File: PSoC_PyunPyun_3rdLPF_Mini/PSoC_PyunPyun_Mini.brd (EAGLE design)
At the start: 57.1 x 52.1 mm, 28 parts, among them IC1 LM358N

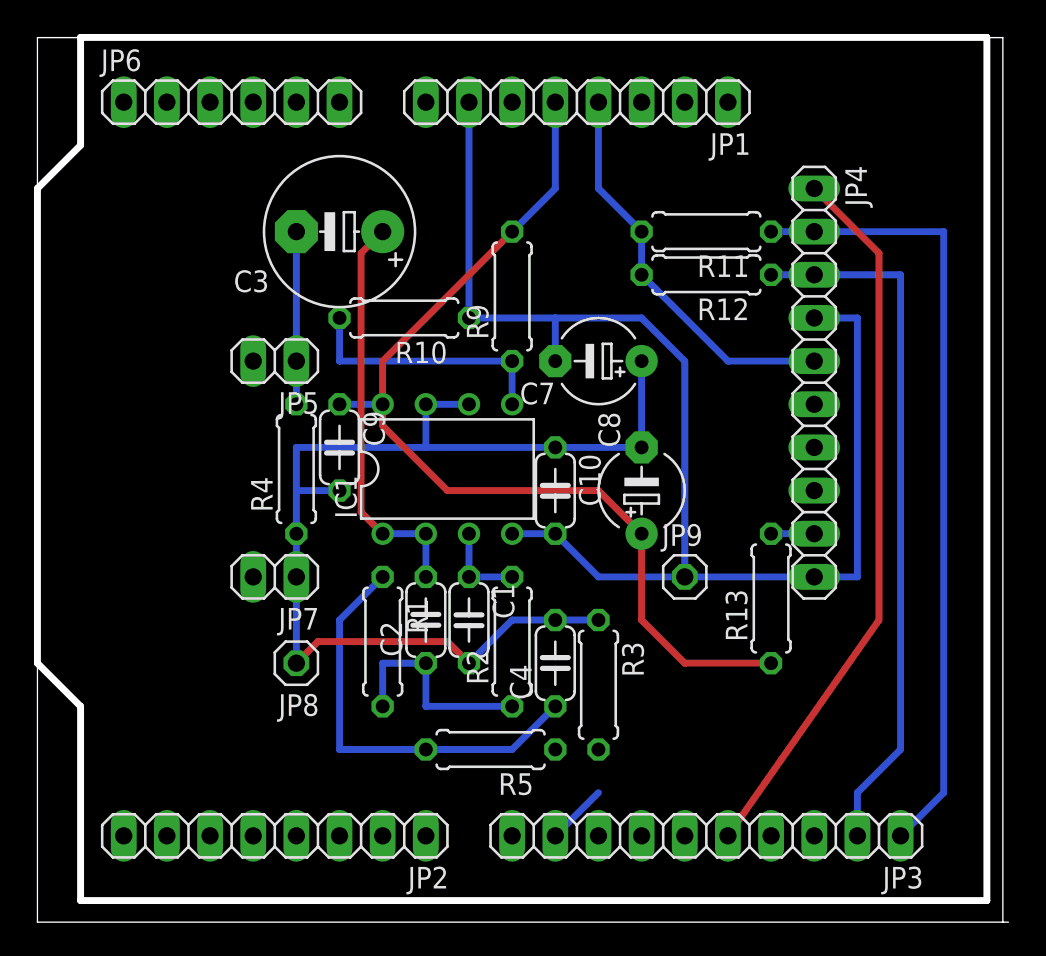
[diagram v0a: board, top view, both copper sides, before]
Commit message: PSoC_Pyun_Pyun_Mini 回路図、基板図修正
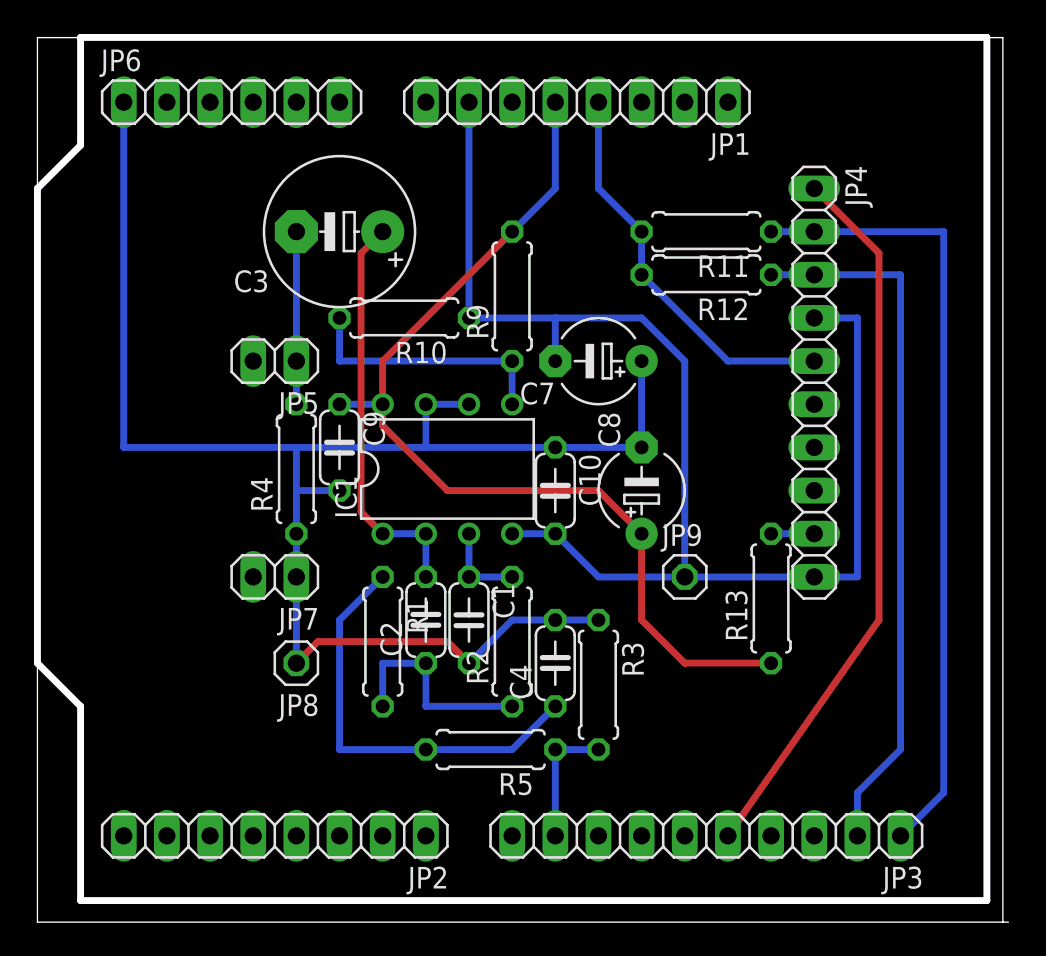
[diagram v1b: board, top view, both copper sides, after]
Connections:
- net AGND: now also JP6.1
- net IDAC7: now also JP3.8; no longer JP3.10
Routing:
- net AGND: track 65.6 -> 96.1 mm
- net IDAC8: track 3.59 -> 7.62 mm
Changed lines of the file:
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@@
 <layer number="97" name="Info" color="7" fill="1" visible="no" active="no"/>
 <layer number="98" name="Guide" color="6" fill="1" visible="no" active="no"/>
-<layer number="100" name="Grid" color="7" fill="1" visible="yes" active="yes"/>
+<layer number="100" name="Grid" color="7" fill="1" visible="no" active="yes"/>
 </layers>
 <board>
@@
 <signal name="IDAC8">
 <contactref element="JP3" pad="9"/>
-<wire x1="30.48" y1="5.08" x2="33.02" y2="7.62" width="0.4064" layer="16"/>
 <contactref element="R5" pad="1"/>
 <contactref element="R3" pad="2"/>
-<wire x1="30.48" y1="10.16" x2="33.02" y2="10.16" width="0" layer="19" extent="1-1"/>
-<wire x1="33.02" y1="7.62" x2="33.02" y2="10.16" width="0" layer="19" extent="16-16"/>
+<wire x1="33.02" y1="10.16" x2="30.48" y2="10.16" width="0.4064" layer="16"/>
+<wire x1="30.48" y1="10.16" x2="30.48" y2="5.08" width="0.4064" layer="16"/>
 </signal>
 <signal name="N$3">
@@
 <wire x1="25.4" y1="15.24" x2="27.94" y2="17.78" width="0.4064" layer="16"/>
 <wire x1="27.94" y1="17.78" x2="30.48" y2="17.78" width="0.4064" layer="16"/>
+<contactref element="JP6" pad="1"/>
+<wire x1="15.24" y1="27.94" x2="5.08" y2="27.94" width="0.4064" layer="16"/>
+<wire x1="5.08" y1="27.94" x2="5.08" y2="48.26" width="0.4064" layer="16"/>
 </signal>
 <signal name="+3.3V">
@@
 </signal>
 <signal name="IDAC7">
-<contactref element="JP3" pad="10"/>
+<contactref element="JP3" pad="8"/>
 </signal>
 </signals>

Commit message: PSoC_Pyun_Pyun_3rdLPF_Mini: Change LCD to aitendo
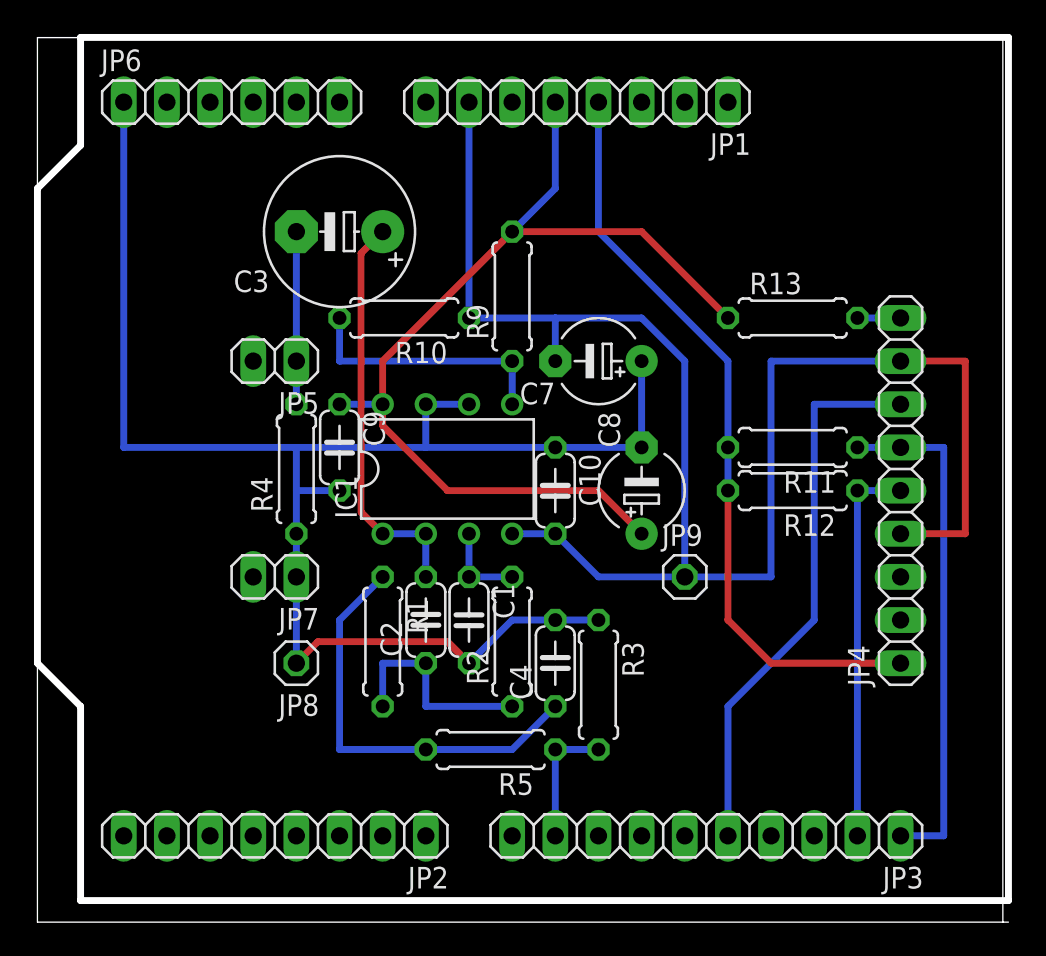
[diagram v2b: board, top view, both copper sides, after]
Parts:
- JP4: value I2C-LCD -> (none); device pinhead:1X10 -> pinhead:1X09
- moved R13 16.6 mm to (44.5, 35.6), turned to 0 degrees
- moved R12 13.7 mm to (44.5, 25.4)
- moved R11 13.7 mm to (44.5, 27.9)
- moved JP4 8.13 mm to (50.8, 25.4), turned to 90 degrees
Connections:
- net +3.3V: now also JP4.1; no longer JP4.5
- net GND: now also JP4.8; no longer JP4.10
- net RST: now also JP4.7; no longer JP4.1
- net SCL: now also JP4.6; no longer JP4.2
- net SDA: now also JP4.5; no longer JP4.3
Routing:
- net +3.3V: track 23.5 -> 44.8 mm
- net SDA: track 41.7 -> 22.9 mm
- net SCL: track 46.8 -> 30.5 mm
- net GND: track 80.8 -> 96.1 mm
- net RST: track 42.5 -> 32.6 mm
- net +5V: track 57.4 -> 58.5 mm
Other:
- outline, holes or cut-outs redrawn
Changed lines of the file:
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@@
 <wire x1="0" y1="43.18" x2="2.54" y2="45.72" width="0.4064" layer="20"/>
 <wire x1="2.54" y1="45.72" x2="2.54" y2="52.07" width="0.4064" layer="20"/>
-<wire x1="2.54" y1="52.07" x2="55.88" y2="52.07" width="0.4064" layer="20"/>
-<wire x1="55.88" y1="52.07" x2="55.88" y2="1.27" width="0.4064" layer="20"/>
-<wire x1="55.88" y1="1.27" x2="2.54" y2="1.27" width="0.4064" layer="20"/>
+<wire x1="2.54" y1="52.07" x2="57.15" y2="52.07" width="0.4064" layer="20"/>
+<wire x1="57.15" y1="52.07" x2="57.15" y2="1.27" width="0.4064" layer="20"/>
+<wire x1="57.15" y1="1.27" x2="2.54" y2="1.27" width="0.4064" layer="20"/>
 <wire x1="2.54" y1="1.27" x2="2.54" y2="12.7" width="0.4064" layer="20"/>
 <wire x1="2.54" y1="12.7" x2="0" y2="15.24" width="0.4064" layer="20"/>
@@
 <element name="JP2" library="pinhead" package="1X08" value="" x="13.97" y="5.08" rot="R180"/>
 <element name="JP3" library="pinhead" package="1X10" value="" x="39.37" y="5.08" rot="R180"/>
-<element name="JP4" library="pinhead" package="1X10" value="I2C-LCD" x="45.72" y="31.75" rot="R270"/>
 <element name="JP5" library="pinhead" package="1X02" value="RCA_HOT" x="13.97" y="33.02" rot="R180"/>
 <element name="R1" library="rcl" package="0207/7" value="100k" x="20.32" y="16.51" rot="R270"/>
 <element name="R10" library="rcl" package="0207/7" value="10k" x="21.59" y="35.56" rot="R180"/>
-<element name="R11" library="rcl" package="0207/7" value="3.3k" x="39.37" y="40.64" rot="R180"/>
-<element name="R12" library="rcl" package="0207/7" value="3.3k" x="39.37" y="38.1" rot="R180"/>
-<element name="R13" library="rcl" package="0207/7" value="330" x="43.18" y="19.05" rot="R90"/>
+<element name="R11" library="rcl" package="0207/7" value="3.3k" x="44.45" y="27.94" rot="R180"/>
+<element name="R12" library="rcl" package="0207/7" value="3.3k" x="44.45" y="25.4" rot="R180"/>
+<element name="R13" library="rcl" package="0207/7" value="330" x="44.45" y="35.56"/>
 <element name="R2" library="rcl" package="0207/7" value="33k" x="27.94" y="16.51" rot="R90"/>
 <element name="R3" library="rcl" package="0207/7" value="2.2k" x="33.02" y="13.97" rot="R270"/>
@@
 <element name="JP8" library="pinhead" package="1X01" value="TP-VGND" x="15.24" y="15.24" rot="R180"/>
 <element name="JP9" library="pinhead" package="1X01" value="TP-GND" x="38.1" y="20.32"/>
+<element name="JP4" library="pinhead" package="1X09" value="" x="50.8" y="25.4" rot="R90"/>
 </elements>
 <signals>
@@
 <contactref element="JP1" pad="7"/>
 <contactref element="C7" pad="-"/>
-<contactref element="JP4" pad="4"/>
-<contactref element="JP4" pad="10"/>
 <contactref element="IC1" pad="4"/>
 <contactref element="C10" pad="2"/>
 <contactref element="JP9" pad="1"/>
-<wire x1="45.72" y1="35.56" x2="48.26" y2="35.56" width="0.4064" layer="16"/>
-<wire x1="48.26" y1="35.56" x2="48.26" y2="20.32" width="0.4064" layer="16"/>
-<wire x1="48.26" y1="20.32" x2="45.72" y2="20.32" width="0.4064" layer="16"/>
 <wire x1="27.94" y1="22.86" x2="30.48" y2="22.86" width="0.4064" layer="16"/>
 <wire x1="25.4" y1="48.26" x2="25.4" y2="35.56" width="0.4064" layer="16"/>
@@
 <wire x1="30.48" y1="35.56" x2="35.56" y2="35.56" width="0.4064" layer="16"/>
 <wire x1="30.48" y1="33.02" x2="30.48" y2="35.56" width="0.4064" layer="16"/>
-<wire x1="45.72" y1="20.32" x2="38.1" y2="20.32" width="0.4064" layer="16"/>
 <wire x1="30.48" y1="22.86" x2="33.02" y2="20.32" width="0.4064" layer="16"/>
 <wire x1="33.02" y1="20.32" x2="38.1" y2="20.32" width="0.4064" layer="16"/>
+<contactref element="JP4" pad="4"/>
+<contactref element="JP4" pad="8"/>
+<wire x1="50.8" y1="33.02" x2="43.18" y2="33.02" width="0.4064" layer="16"/>
+<wire x1="43.18" y1="33.02" x2="43.18" y2="20.32" width="0.4064" layer="16"/>
+<wire x1="43.18" y1="20.32" x2="38.1" y2="20.32" width="0.4064" layer="16"/>
+<wire x1="50.8" y1="22.86" x2="54.61" y2="22.86" width="0.4064" layer="1"/>
+<wire x1="54.61" y1="22.86" x2="54.61" y2="33.02" width="0.4064" layer="1"/>
+<wire x1="54.61" y1="33.02" x2="50.8" y2="33.02" width="0.4064" layer="1"/>
 </signal>
 <signal name="N$8">
@@
 <contactref element="C9" pad="1"/>
 <contactref element="IC1" pad="8"/>
-<wire x1="30.48" y1="48.26" x2="30.48" y2="43.18" width="0.4064" layer="16"/>
-<wire x1="30.48" y1="43.18" x2="27.94" y2="40.64" width="0.4064" layer="16"/>
 <wire x1="17.78" y1="30.48" x2="20.32" y2="30.48" width="0.4064" layer="16"/>
-<wire x1="35.56" y1="22.86" x2="35.56" y2="17.78" width="0.4064" layer="1"/>
-<wire x1="35.56" y1="17.78" x2="38.1" y2="15.24" width="0.4064" layer="1"/>
-<wire x1="38.1" y1="15.24" x2="43.18" y2="15.24" width="0.4064" layer="1"/>
 <wire x1="35.56" y1="22.86" x2="33.02" y2="25.4" width="0.4064" layer="1"/>
 <wire x1="33.02" y1="25.4" x2="24.13" y2="25.4" width="0.4064" layer="1"/>
@@
 <wire x1="20.32" y1="30.48" x2="20.32" y2="33.02" width="0.4064" layer="1"/>
 <wire x1="20.32" y1="33.02" x2="27.94" y2="40.64" width="0.4064" layer="1"/>
+<wire x1="30.48" y1="48.26" x2="30.48" y2="43.18" width="0.4064" layer="16"/>
+<wire x1="30.48" y1="43.18" x2="27.94" y2="40.64" width="0.4064" layer="16"/>
+<wire x1="40.64" y1="35.56" x2="35.56" y2="40.64" width="0.4064" layer="1"/>
+<wire x1="35.56" y1="40.64" x2="27.94" y2="40.64" width="0.4064" layer="1"/>
 </signal>
 <signal name="AGND">
@@
 <signal name="+3.3V">
 <contactref element="JP1" pad="4"/>
-<contactref element="JP4" pad="5"/>
 <contactref element="R11" pad="2"/>
 <contactref element="R12" pad="2"/>
-<wire x1="33.02" y1="48.26" x2="33.02" y2="43.18" width="0.4064" layer="16"/>
-<wire x1="33.02" y1="43.18" x2="35.56" y2="40.64" width="0.4064" layer="16"/>
-<wire x1="35.56" y1="40.64" x2="35.56" y2="38.1" width="0.4064" layer="16"/>
-<wire x1="35.56" y1="38.1" x2="40.64" y2="33.02" width="0.4064" layer="16"/>
-<wire x1="40.64" y1="33.02" x2="45.72" y2="33.02" width="0.4064" layer="16"/>
+<wire x1="40.64" y1="27.94" x2="40.64" y2="25.4" width="0.4064" layer="16"/>
+<contactref element="JP4" pad="1"/>
+<wire x1="40.64" y1="27.94" x2="40.64" y2="33.02" width="0.4064" layer="16"/>
+<wire x1="40.64" y1="33.02" x2="33.02" y2="40.64" width="0.4064" layer="16"/>
+<wire x1="33.02" y1="40.64" x2="33.02" y2="48.26" width="0.4064" layer="16"/>
+<wire x1="50.8" y1="15.24" x2="43.18" y2="15.24" width="0.4064" layer="1"/>
+<wire x1="43.18" y1="15.24" x2="40.64" y2="17.78" width="0.4064" layer="1"/>
+<wire x1="40.64" y1="17.78" x2="40.64" y2="25.4" width="0.4064" layer="1"/>
 </signal>
 <signal name="RST">
-<contactref element="JP4" pad="1"/>
 <contactref element="JP3" pad="5"/>
-<wire x1="45.72" y1="43.18" x2="49.53" y2="39.37" width="0.4064" layer="1"/>
-<wire x1="49.53" y1="39.37" x2="49.53" y2="17.78" width="0.4064" layer="1"/>
-<wire x1="49.53" y1="17.78" x2="40.64" y2="5.08" width="0.4064" layer="1"/>
+<contactref element="JP4" pad="7"/>
+<wire x1="40.64" y1="5.08" x2="40.64" y2="12.7" width="0.4064" layer="16"/>
+<wire x1="40.64" y1="12.7" x2="45.72" y2="17.78" width="0.4064" layer="16"/>
+<wire x1="45.72" y1="17.78" x2="45.72" y2="30.48" width="0.4064" layer="16"/>
+<wire x1="45.72" y1="30.48" x2="50.8" y2="30.48" width="0.4064" layer="16"/>
 </signal>
 <signal name="SCL">
 <contactref element="JP3" pad="1"/>
-<contactref element="JP4" pad="2"/>
 <contactref element="R11" pad="1"/>
-<wire x1="45.72" y1="40.64" x2="43.18" y2="40.64" width="0.4064" layer="16"/>
-<wire x1="53.34" y1="40.64" x2="45.72" y2="40.64" width="0.4064" layer="16"/>
-<wire x1="50.8" y1="5.08" x2="53.34" y2="7.62" width="0.4064" layer="16"/>
-<wire x1="53.34" y1="7.62" x2="53.34" y2="40.64" width="0.4064" layer="16"/>
+<contactref element="JP4" pad="6"/>
+<wire x1="48.26" y1="27.94" x2="50.8" y2="27.94" width="0.4064" layer="16"/>
+<wire x1="53.34" y1="5.08" x2="53.34" y2="27.94" width="0.4064" layer="16"/>
+<wire x1="53.34" y1="27.94" x2="50.8" y2="27.94" width="0.4064" layer="16"/>
+<wire x1="50.8" y1="5.08" x2="53.34" y2="5.08" width="0.4064" layer="16"/>
 </signal>
 <signal name="SDA">
 <contactref element="JP3" pad="2"/>
-<contactref element="JP4" pad="3"/>
 <contactref element="R12" pad="1"/>
-<wire x1="43.18" y1="38.1" x2="45.72" y2="38.1" width="0.4064" layer="16"/>
-<wire x1="48.26" y1="5.08" x2="48.26" y2="7.62" width="0.4064" layer="16"/>
-<wire x1="48.26" y1="7.62" x2="50.8" y2="10.16" width="0.4064" layer="16"/>
-<wire x1="50.8" y1="10.16" x2="50.8" y2="38.1" width="0.4064" layer="16"/>
-<wire x1="50.8" y1="38.1" x2="45.72" y2="38.1" width="0.4064" layer="16"/>
+<contactref element="JP4" pad="5"/>
+<wire x1="48.26" y1="5.08" x2="48.26" y2="25.4" width="0.4064" layer="16"/>
+<wire x1="48.26" y1="25.4" x2="50.8" y2="25.4" width="0.4064" layer="16"/>
 </signal>
 <signal name="N$5">
 <contactref element="R13" pad="2"/>
 <contactref element="JP4" pad="9"/>
-<wire x1="45.72" y1="22.86" x2="43.18" y2="22.86" width="0.4064" layer="16"/>
+<wire x1="48.26" y1="35.56" x2="50.8" y2="35.56" width="0.4064" layer="16"/>
 </signal>
 <signal name="N$2">
